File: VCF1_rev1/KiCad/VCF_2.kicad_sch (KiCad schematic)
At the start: 27 parts, among them U10 CEM3350, U11 Opamp_Quad, U12 74HC4053, U9 74HC4053

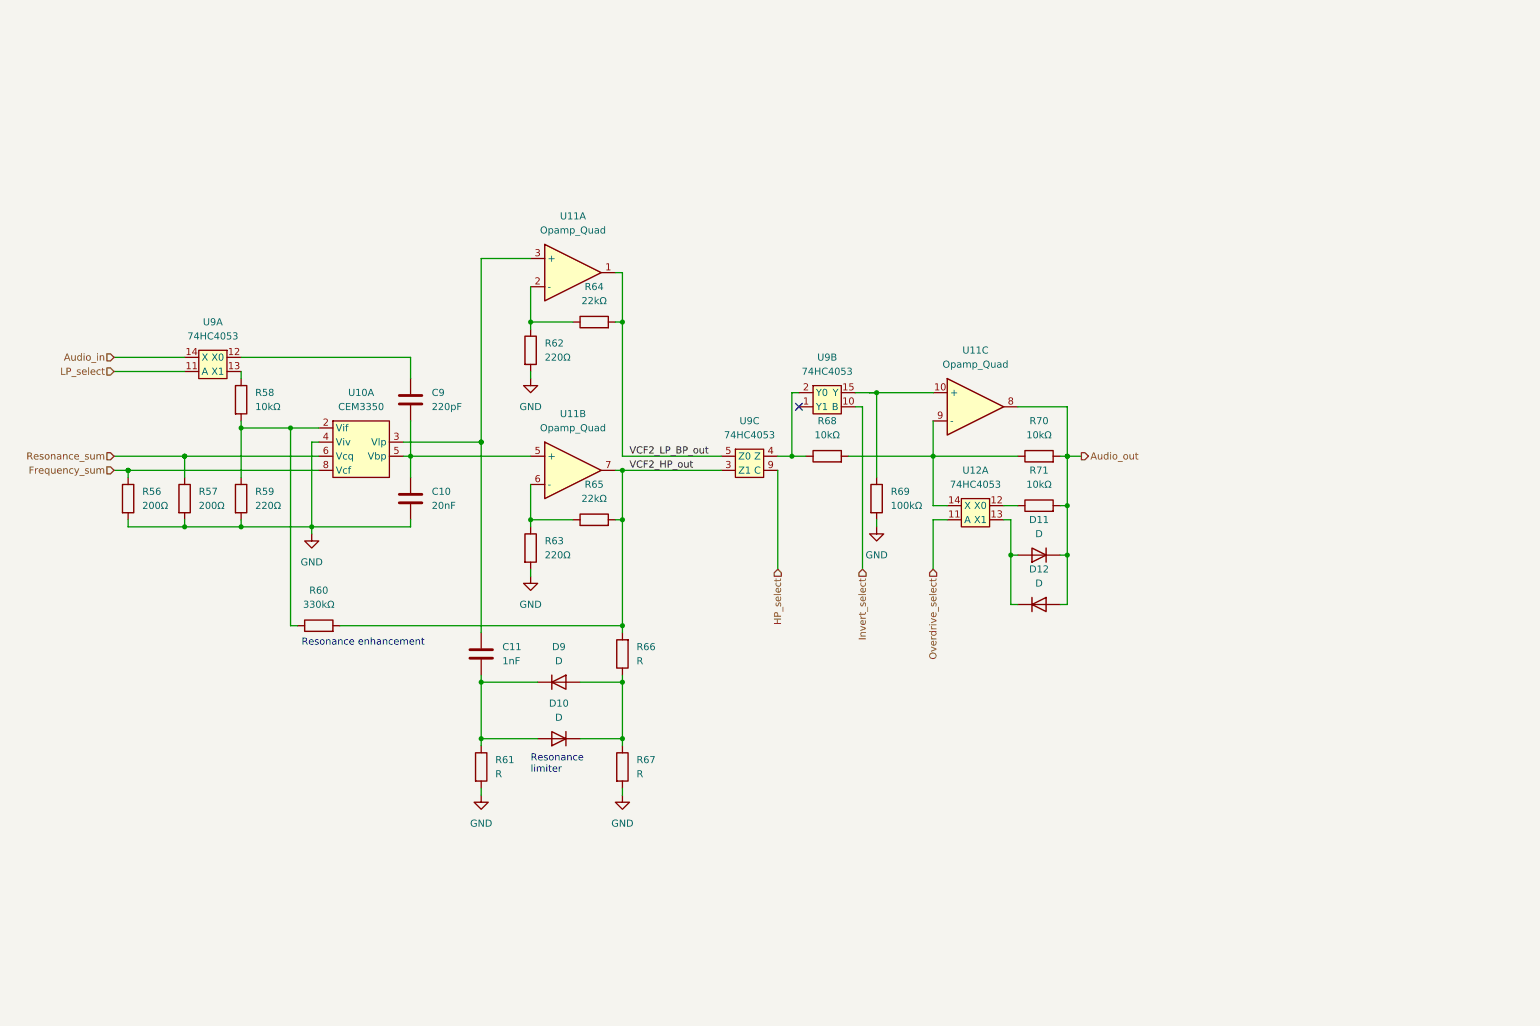
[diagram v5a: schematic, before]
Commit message: Cleaned up the first page with the overview and tried to make it a bit more readable.
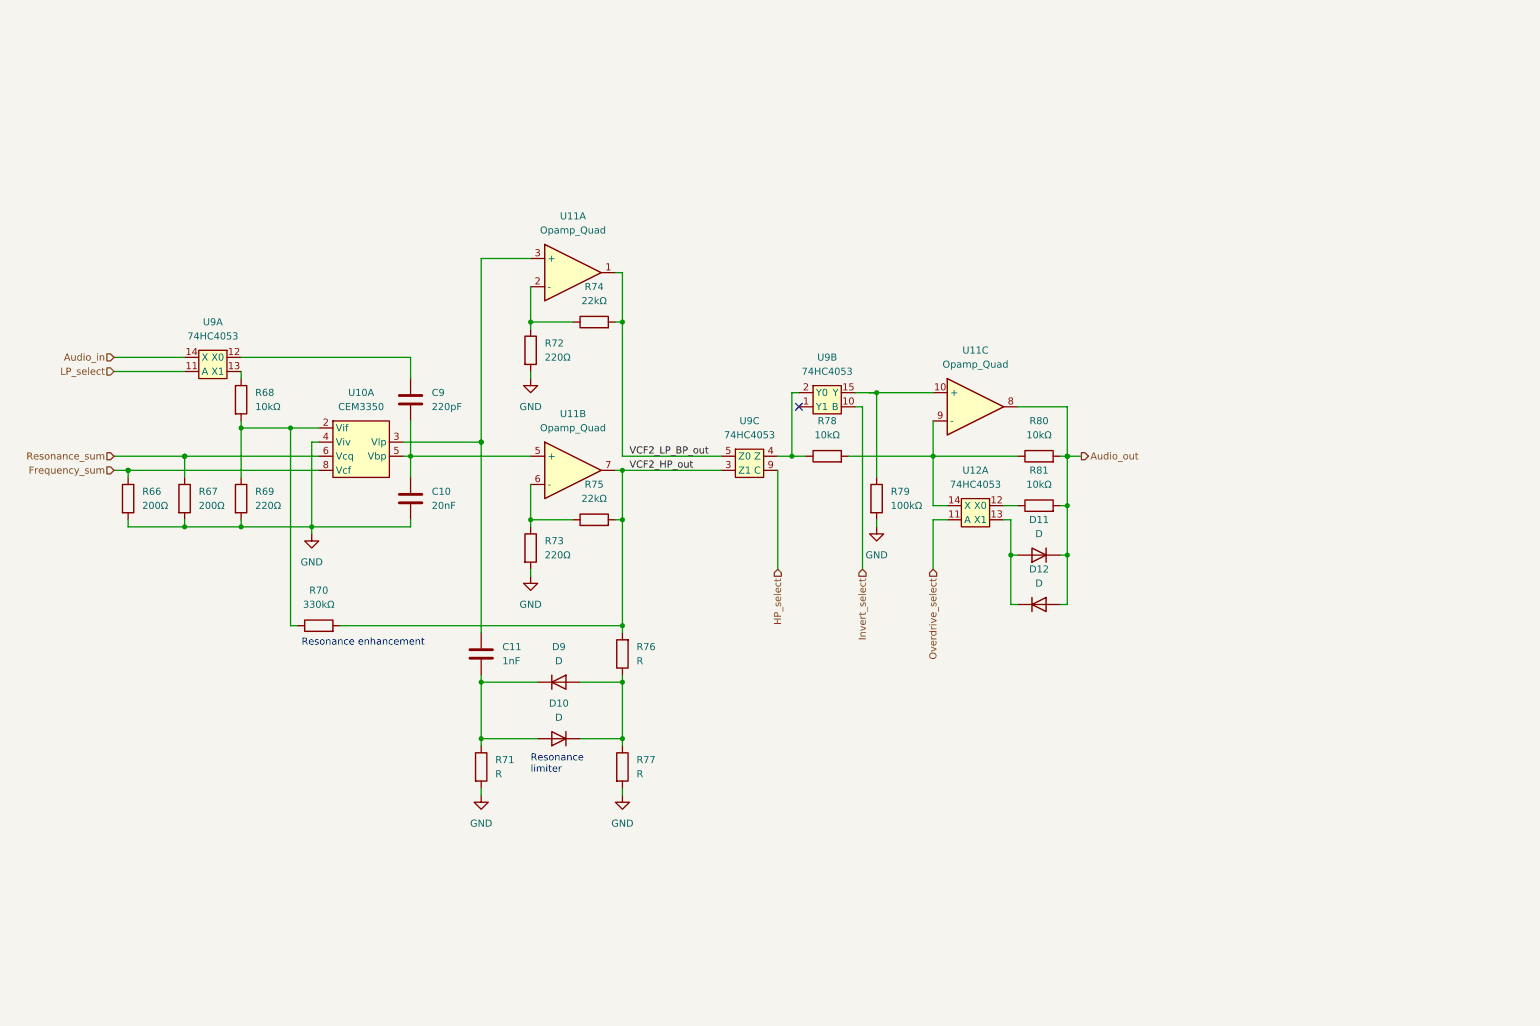
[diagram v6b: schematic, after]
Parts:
- renumbered R56 to R66, R57 to R67, R58 to R68, R59 to R69, R60 to R70, R61 to R71, R62 to R72, R63 to R73, R64 to R74, R65 to R75, R66 to R76, R67 to R77, R68 to R78, R69 to R79, R70 to R80, R71 to R81

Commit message: Drew a better symbol for LM13700 because the other one was ugly.
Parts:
- R66, R67, R68, R69, R70, R71, R72, R73, R74, R75, R76, R77, R78, R79, R80, R81: footprint (none) -> Resistor_SMD:R_0603_1608Metric
